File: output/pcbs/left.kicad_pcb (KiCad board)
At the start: 2 copper layers, 121.3 x 90.2 mm, 19 parts

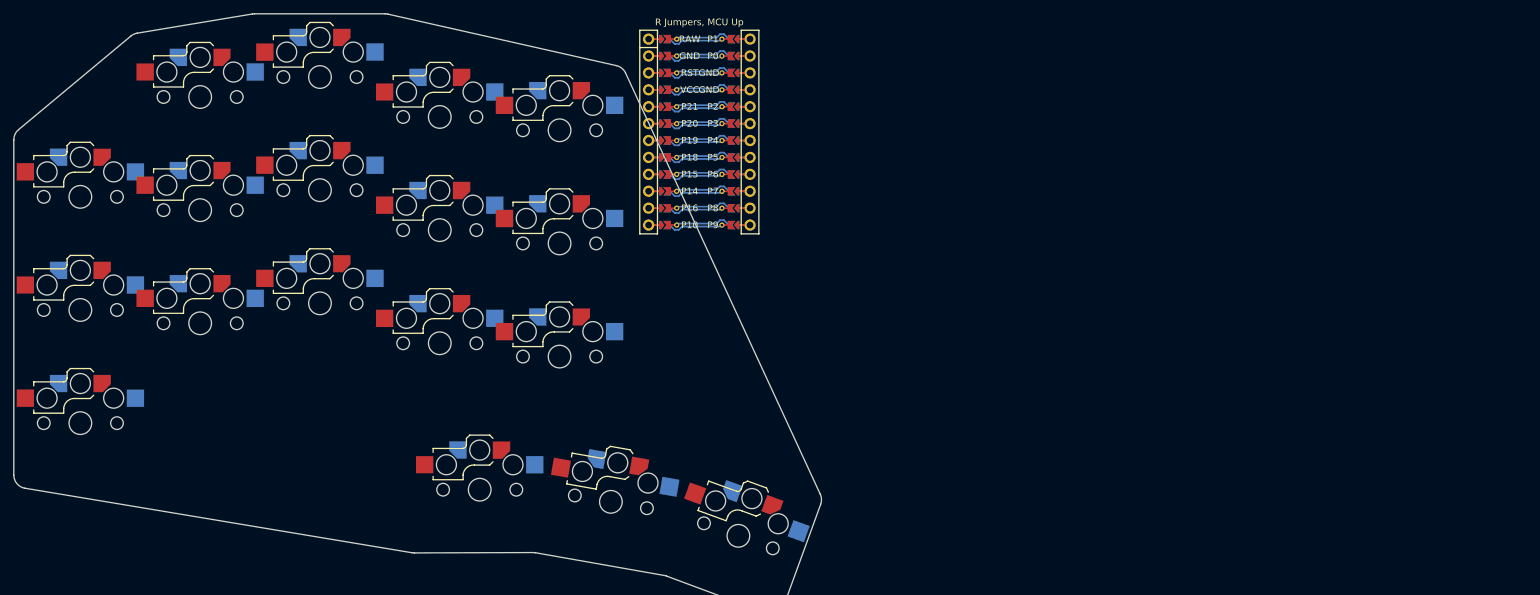
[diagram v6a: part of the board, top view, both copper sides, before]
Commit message: Undo reversibleness and mirror the sides
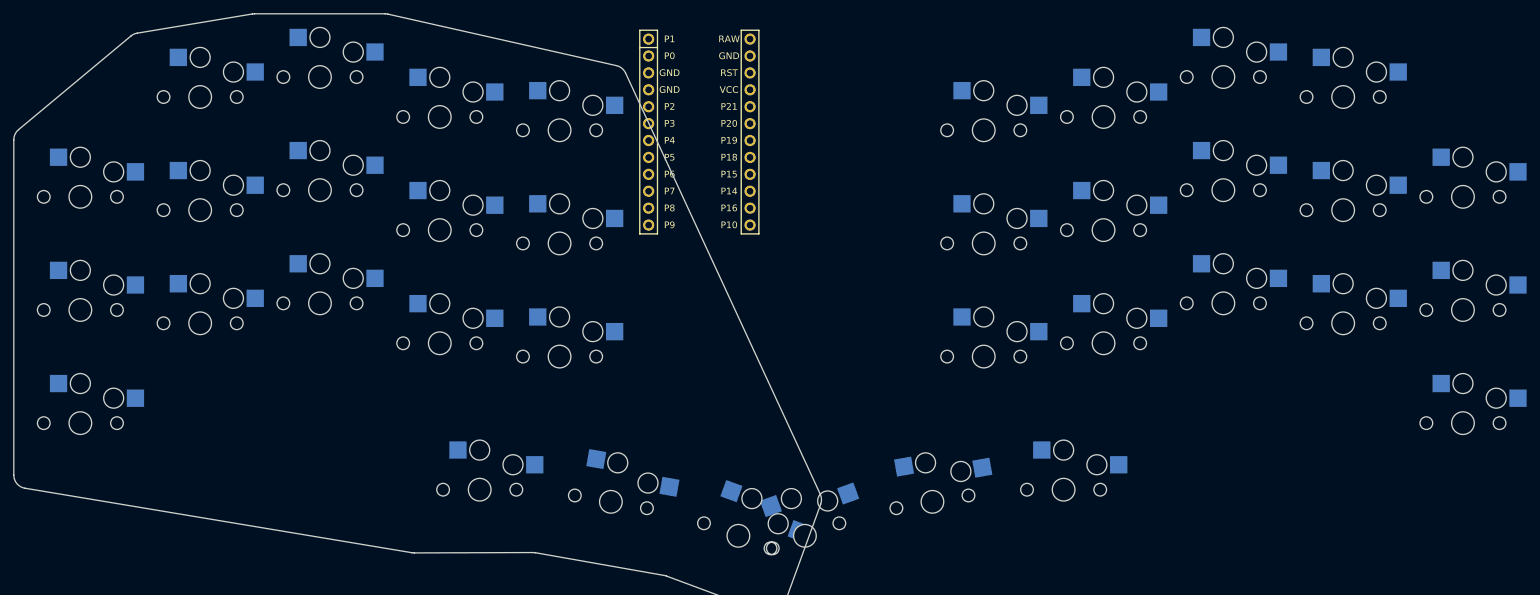
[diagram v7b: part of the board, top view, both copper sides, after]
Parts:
- added S19: , ceoloide:switch_choc_v1_v2, B.Cu at (207.7, 0.00)
- added S20: , ceoloide:switch_choc_v1_v2, B.Cu at (207.7, -17.0)
- added S21: , ceoloide:switch_choc_v1_v2, B.Cu at (207.7, -34.0)
- added S22: , ceoloide:switch_choc_v1_v2, B.Cu at (189.7, -15.0)
- added S23: , ceoloide:switch_choc_v1_v2, B.Cu at (189.7, -32.0)
- added S24: , ceoloide:switch_choc_v1_v2, B.Cu at (189.7, -49.0)
- added S25: , ceoloide:switch_choc_v1_v2, B.Cu at (171.7, -18.0)
- added S26: , ceoloide:switch_choc_v1_v2, B.Cu at (171.7, -35.0)
- added S27: , ceoloide:switch_choc_v1_v2, B.Cu at (171.7, -52.0)
- added S28: , ceoloide:switch_choc_v1_v2, B.Cu at (153.7, -12.0)
- added S29: , ceoloide:switch_choc_v1_v2, B.Cu at (153.7, -29.0)
- added S30: , ceoloide:switch_choc_v1_v2, B.Cu at (153.7, -46.0)
- added S31: , ceoloide:switch_choc_v1_v2, B.Cu at (135.7, -10.0)
- added S32: , ceoloide:switch_choc_v1_v2, B.Cu at (135.7, -27.0)
- added S33: , ceoloide:switch_choc_v1_v2, B.Cu at (135.7, -44.0)
- added S34: , ceoloide:switch_choc_v1_v2, B.Cu at (147.7, 10.0)
- added S35: , ceoloide:switch_choc_v1_v2, B.Cu at (128.0, 11.8)
- added S36: , ceoloide:switch_choc_v1_v2, B.Cu at (108.9, 16.9)
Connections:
- MCU1 pad 1: MCU1_1 -> RAW
- MCU1 pad 10: MCU1_10 -> P14
- MCU1 pad 11: MCU1_11 -> P16
- MCU1 pad 12: MCU1_12 -> P10
- MCU1 pad 13: MCU1_13 -> P9
- MCU1 pad 14: MCU1_14 -> P8
- MCU1 pad 15: MCU1_15 -> P7
- MCU1 pad 16: MCU1_16 -> P6
- MCU1 pad 17: MCU1_17 -> P5
- MCU1 pad 18: MCU1_18 -> P4
- MCU1 pad 19: MCU1_19 -> P3
- MCU1 pad 2: MCU1_2 -> GND
- MCU1 pad 20: MCU1_20 -> P2
- MCU1 pad 21: MCU1_21 -> GND
- MCU1 pad 22: MCU1_22 -> GND
- MCU1 pad 23: MCU1_23 -> P0
- MCU1 pad 24: MCU1_24 -> P1
- MCU1 pad 3: MCU1_3 -> RST
- MCU1 pad 4: MCU1_4 -> VCC
- MCU1 pad 5: MCU1_5 -> P21
- MCU1 pad 6: MCU1_6 -> P20
- MCU1 pad 7: MCU1_7 -> P19
- MCU1 pad 8: MCU1_8 -> P18
- MCU1 pad 9: MCU1_9 -> P15
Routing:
- net (no net): track 337.7 -> 0.00 mm

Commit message: Spacing
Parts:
- moved S36 23.3 mm to (131.0, 24.3), turned to 26 degrees
- moved S35 22.2 mm to (149.5, 17.2), turned to 16 degrees
- moved S34 21.5 mm to (168.9, 13.3), turned to 6 degrees
- moved S31 19.7 mm to (154.9, -5.33), turned to 6 degrees
- moved S28 19.1 mm to (172.6, -9.21), turned to 6 degrees
- moved S19 18.3 mm to (226.0, 0.00)
- moved S20 18.3 mm to (226.0, -17.0)
- moved S21 18.3 mm to (226.0, -34.0)
- moved S22 18.3 mm to (208.0, -15.0), turned to 3 degrees
- moved S25 18.2 mm to (189.9, -17.1), turned to 6 degrees
- moved S32 18.0 mm to (153.1, -22.2), turned to 6 degrees
- moved S23 17.4 mm to (207.1, -32.0), turned to 3 degrees
- moved S29 17.3 mm to (170.8, -26.1), turned to 6 degrees
- moved S24 16.5 mm to (206.2, -49.0), turned to 3 degrees
- moved S26 16.4 mm to (188.1, -34.0), turned to 6 degrees
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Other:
- board size 121.3 x 90.2 mm -> 118.1 x 97.8 mm
